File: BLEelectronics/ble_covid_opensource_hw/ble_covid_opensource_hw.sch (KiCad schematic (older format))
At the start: 35 parts, among them IC1 LTC4412xS6, IC2 LTC4054LES5-4.2#TRPBF, IC3 PCF8523T, IC4 MX25R6435FM2IL0, J1 USB_B_Micro, Q1 Si2307CDS, U1 BAT-HLD-001, U2 ESD401, U3 ESD401, U4 LP5907MFX-3.3

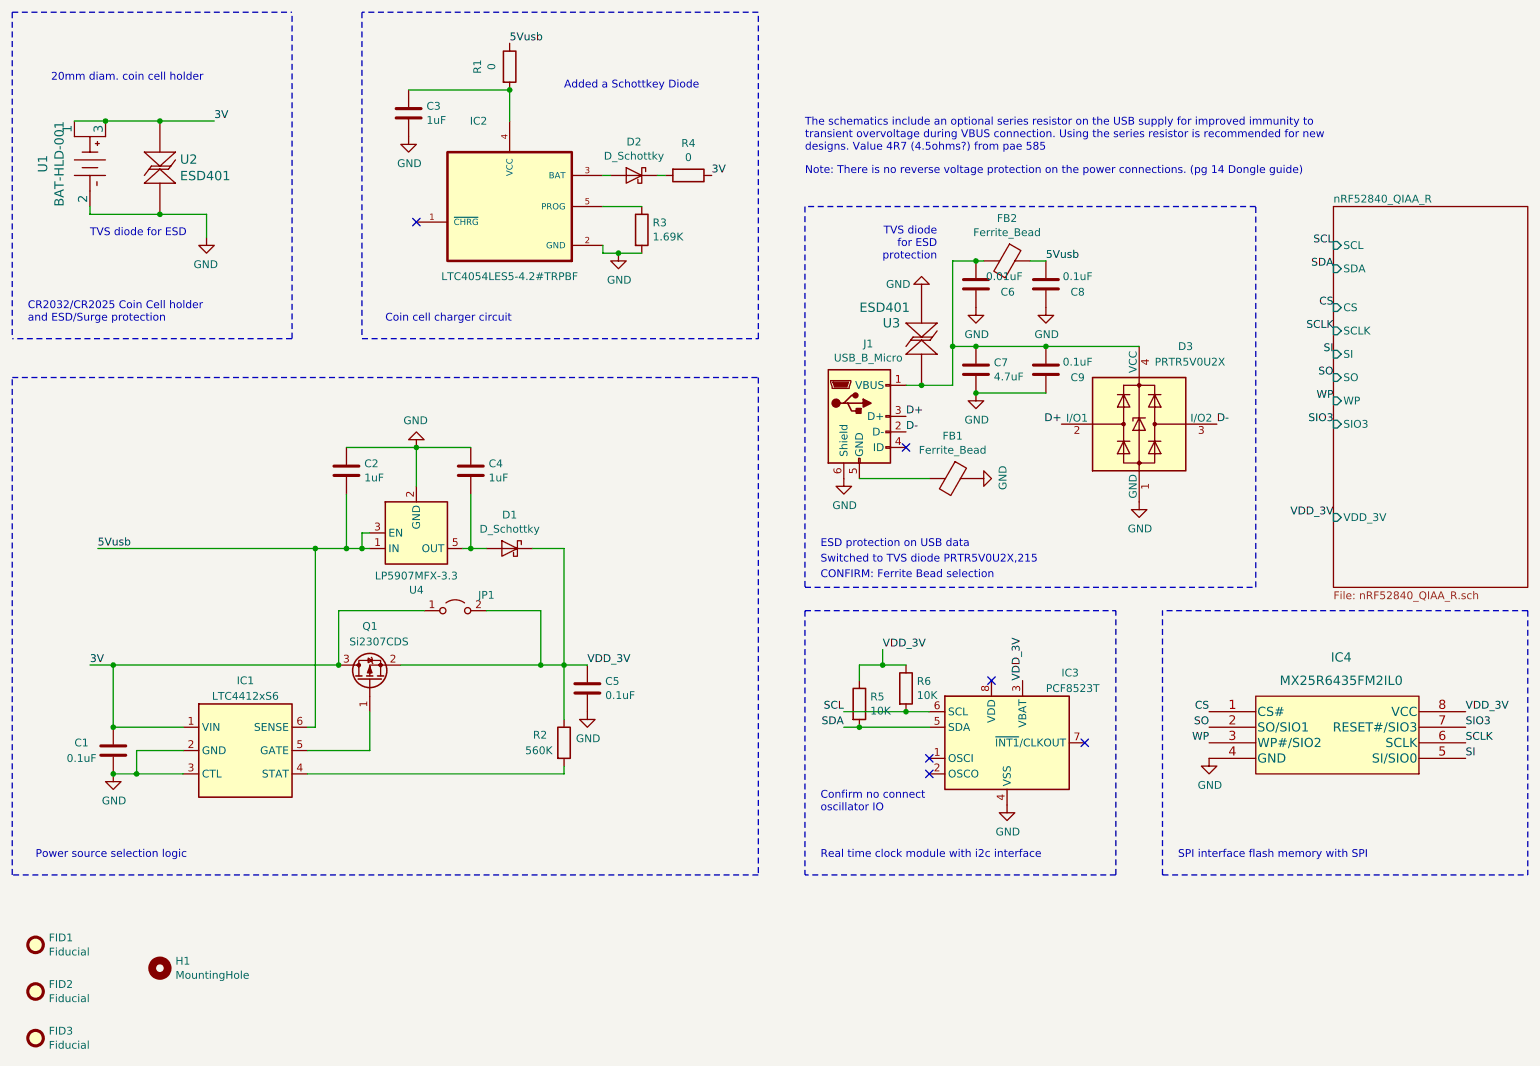
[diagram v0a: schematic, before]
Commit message: Moved power from pin 3 VBat to pin 8 Vdd on RTC. Swapped SIO3 and SDA on 1a and 1b. Changed battery footprint to allow backside routing for Flash and USB data. Todo: Unbreak MVP1B layout rerouting.
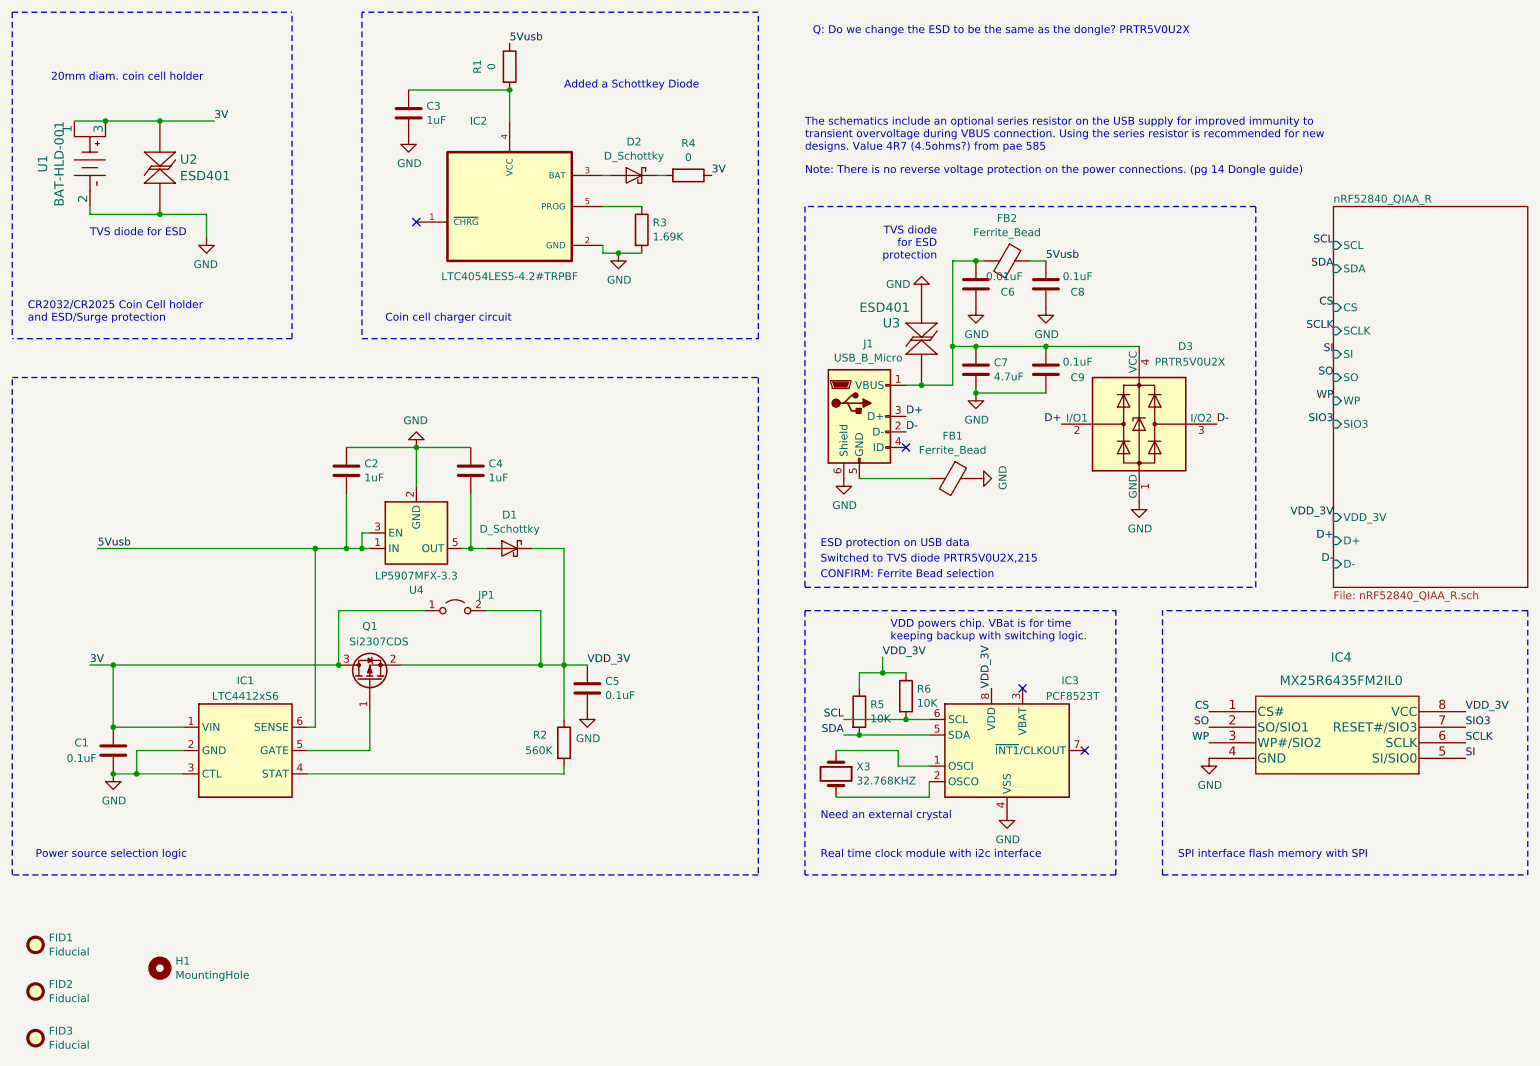
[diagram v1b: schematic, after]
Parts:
- added X3: 32.768KHZ, Crystal:Crystal_SMD_3215-2Pin_3.2x1.5mm, symbol Device:Crystal
- U1: footprint 0my_footprints:BAT-HLD-001 -> 0my_footprints:BAT-HLD-001_smallerGND
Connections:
- net VDD_3V: now also IC3.8 (VDD); no longer IC3.3 (VBAT)
- net at IC3.1 (OSCI): now also X3.1
- net at IC3.2 (OSCO): now also X3.2
- no-connect marks 6 -> 4
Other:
- note added: "Need an external crystal"
- note added: "Q: Do we change the ESD to be the same as the dongle? PRTR5V0U2X"
- note added: "VDD powers chip. VBat is for time \nkeeping backup with switching logic."
- note removed: "Confirm no connect\noscillator IO"
- moved on the sheet: IC3, R5, R6
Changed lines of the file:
@@
 F 0 "U1" H 1725 1803 60  0000 C CNN
 F 1 "BAT-HLD-001" H 1725 1697 60  0000 C CNN
-F 2 "0my_footprints:BAT-HLD-001" H 1734 1258 60  0001 C CNN
+F 2 "0my_footprints:BAT-HLD-001_smallerGND" H 1734 1258 60  0001 C CNN
 F 3 "https://linxtechnologies.com/wp/wp-content/uploads/catalog-battery-holders.pdf" H 1450 1600 60  0001 C CNN
 F 4 "Linx Technologies Inc." H -200 -100 50  0001 C CNN "MFR"
@@
 L Timer_RTC:PCF8523T IC3
 U 1 1 5E9F84DB
-P 7450 5600
-F 0 "IC3" H 7800 6050 50  0000 L CNN
-F 1 "PCF8523T" H 7700 5950 50  0000 L CNN
-F 2 "Package_SO:SOIC-8_3.9x4.9mm_P1.27mm" H 8250 5250 50  0001 C CNN
-F 3 "https://www.nxp.com/docs/en/data-sheet/PCF8523.pdf" H 7450 5600 50  0001 C CNN
-F 4 "NXP USA Inc." H 300 1500 50  0001 C CNN "MFR"
-F 5 "PCF8523T/1,118" H 300 1500 50  0001 C CNN "MPN"
-F 6 "568-5306-1-ND" H 300 1500 50  0001 C CNN "DPN"
-F 7 "-" H 300 1500 50  0001 C CNN "LCSCPN"
-F 8 "-" H 300 1500 50  0001 C CNN "SPR"
-F 9 "-" H 300 1500 50  0001 C CNN "SPN"
-F 10 "-" H 300 1500 50  0001 C CNN "SIM"
-	1    7450 5600
+P 7450 5650
+F 0 "IC3" H 7800 6100 50  0000 L CNN
+F 1 "PCF8523T" H 7700 6000 50  0000 L CNN
+F 2 "Package_SO:SOIC-8_3.9x4.9mm_P1.27mm" H 8250 5300 50  0001 C CNN
+F 3 "https://www.nxp.com/docs/en/data-sheet/PCF8523.pdf" H 7450 5650 50  0001 C CNN
+F 4 "NXP USA Inc." H 300 1550 50  0001 C CNN "MFR"
+F 5 "PCF8523T/1,118" H 300 1550 50  0001 C CNN "MPN"
+F 6 "568-5306-1-ND" H 300 1550 50  0001 C CNN "DPN"
+F 7 "-" H 300 1550 50  0001 C CNN "LCSCPN"
+F 8 "-" H 300 1550 50  0001 C CNN "SPR"
+F 9 "-" H 300 1550 50  0001 C CNN "SPN"
+F 10 "-" H 300 1550 50  0001 C CNN "SIM"
+	1    7450 5650
 	1    0    0    -1
 $EndComp
@@
 L power:GND #PWR012
 U 1 1 5EA0EA9A
-P 7450 6000
-F 0 "#PWR012" H 7450 5750 50  0001 C CNN
-F 1 "GND" H 7455 5827 50  0000 C CNN
-F 2 "" H 7450 6000 50  0001 C CNN
-F 3 "" H 7450 6000 50  0001 C CNN
-	1    7450 6000
+P 7450 6050
+F 0 "#PWR012" H 7450 5800 50  0001 C CNN
+F 1 "GND" H 7455 5877 50  0000 C CNN
+F 2 "" H 7450 6050 50  0001 C CNN
+F 3 "" H 7450 6050 50  0001 C CNN
+	1    7450 6050
 	1    0    0    -1
 $EndComp
@@
 L Device:R R6
 U 1 1 5EA074F4
-P 6800 5250
-F 0 "R6" H 6870 5296 50  0000 L CNN
-F 1 "10K" H 6870 5205 50  0000 L CNN
-F 2 "Resistor_SMD:R_0402_1005Metric" V 6730 5250 50  0001 C CNN
-F 3 "https://www.yageo.com/upload/media/product/productsearch/datasheet/rchip/PYu-RC_Group_51_RoHS_L_10.pdf" H 6800 5250 50  0001 C CNN
-F 4 "Yageo" H 350 1500 50  0001 C CNN "MFR"
-F 5 "RC0603FR-074K7L" H 350 1500 50  0001 C CNN "MPN"
-F 6 "311-4.70KHRCT-ND" H 350 1500 50  0001 C CNN "DPN"
-F 7 "-" H 350 1500 50  0001 C CNN "LCSCPN"
-F 8 "-" H 350 1500 50  0001 C CNN "SPR"
-F 9 "-" H 350 1500 50  0001 C CNN "SPN"
-F 10 "-" H 350 1500 50  0001 C CNN "SIM"
-	1    6800 5250
+P 6800 5300
+F 0 "R6" H 6870 5346 50  0000 L CNN
+F 1 "10K" H 6870 5255 50  0000 L CNN
+F 2 "Resistor_SMD:R_0402_1005Metric" V 6730 5300 50  0001 C CNN
+F 3 "https://www.yageo.com/upload/media/product/productsearch/datasheet/rchip/PYu-RC_Group_51_RoHS_L_10.pdf" H 6800 5300 50  0001 C CNN
+F 4 "Yageo" H 350 1550 50  0001 C CNN "MFR"
+F 5 "RC0603FR-074K7L" H 350 1550 50  0001 C CNN "MPN"
+F 6 "311-4.70KHRCT-ND" H 350 1550 50  0001 C CNN "DPN"
+F 7 "-" H 350 1550 50  0001 C CNN "LCSCPN"
+F 8 "-" H 350 1550 50  0001 C CNN "SPR"
+F 9 "-" H 350 1550 50  0001 C CNN "SPN"
+F 10 "-" H 350 1550 50  0001 C CNN "SIM"
+	1    6800 5300
 	1    0    0    -1
 $EndComp
@@
 L Device:R R5
 U 1 1 5EA0D031
-P 6500 5350
-F 0 "R5" H 6570 5396 50  0000 L CNN
-F 1 "10K" H 6570 5305 50  0000 L CNN
-F 2 "Resistor_SMD:R_0402_1005Metric" V 6430 5350 50  0001 C CNN
-F 3 "https://www.yageo.com/upload/media/product/productsearch/datasheet/rchip/PYu-RC_Group_51_RoHS_L_10.pdf" H 6500 5350 50  0001 C CNN
-F 4 "Yageo" H 50  1600 50  0001 C CNN "MFR"
-F 5 "RC0603FR-074K7L" H 50  1600 50  0001 C CNN "MPN"
-F 6 "311-4.70KHRCT-ND" H 50  1600 50  0001 C CNN "DPN"
-F 7 "-" H 50  1600 50  0001 C CNN "LCSCPN"
-F 8 "-" H 50  1600 50  0001 C CNN "SPR"
-F 9 "-" H 50  1600 50  0001 C CNN "SPN"
-F 10 "-" H 50  1600 50  0001 C CNN "SIM"
-	1    6500 5350
+P 6500 5400
+F 0 "R5" H 6570 5446 50  0000 L CNN
+F 1 "10K" H 6570 5355 50  0000 L CNN
+F 2 "Resistor_SMD:R_0402_1005Metric" V 6430 5400 50  0001 C CNN
+F 3 "https://www.yageo.com/upload/media/product/productsearch/datasheet/rchip/PYu-RC_Group_51_RoHS_L_10.pdf" H 6500 5400 50  0001 C CNN
+F 4 "Yageo" H 50  1650 50  0001 C CNN "MFR"
+F 5 "RC0603FR-074K7L" H 50  1650 50  0001 C CNN "MPN"
+F 6 "311-4.70KHRCT-ND" H 50  1650 50  0001 C CNN "DPN"
+F 7 "-" H 50  1650 50  0001 C CNN "LCSCPN"
+F 8 "-" H 50  1650 50  0001 C CNN "SPR"
+F 9 "-" H 50  1650 50  0001 C CNN "SPN"
+F 10 "-" H 50  1650 50  0001 C CNN "SIM"
+	1    6500 5400
 	1    0    0    -1
 $EndComp
@@
 Text Label 10400 5400 0    50   ~ 0
 VDD_3V
-Text Label 7550 5200 1    50   ~ 0
+Text Label 7350 5250 1    50   ~ 0
 VDD_3V
 Text Notes 6250 6350 0    50   ~ 0
 Real time clock module with i2c interface
-Text Label 6400 5400 2    50   ~ 0
+Text Label 6400 5450 2    50   ~ 0
 SCL
-Text Label 6400 5500 2    50   ~ 0
+Text Label 6400 5550 2    50   ~ 0
 SDA
 Text Label 8750 5500 2    50   ~ 0
@@
 Text Label 8750 5600 2    50   ~ 0
 WP
-Text Label 6650 5000 0    50   ~ 0
+Text Label 6650 5050 0    50   ~ 0
 VDD_3V
 Text Notes 1550 2350 0    50   ~ 0
 TVS diode for ESD
-Text Notes 6250 6050 0    50   ~ 0
-Confirm no connect\noscillator IO
+Text Notes 6250 6100 0    50   ~ 0
+Need an external crystal
 Text Label 10400 5600 0    50   ~ 0
 SCLK
@@
 	10800 4750 8450 4750
 Wire Wire Line
-	6950 5400 6800 5400
-Wire Wire Line
-	6800 5400 6400 5400
-Wire Wire Line
-	6500 5500 6400 5500
-Wire Wire Line
-	6500 5500 6950 5500
-Wire Wire Line
-	6500 5200 6500 5100
-Wire Wire Line
-	6500 5100 6650 5100
-Wire Wire Line
-	6650 5100 6650 5000
-Wire Wire Line
-	6650 5100 6800 5100
+	6950 5450 6800 5450
+Wire Wire Line
+	6800 5450 6400 5450
+Wire Wire Line
+	6500 5550 6400 5550
+Wire Wire Line
+	6500 5550 6950 5550
+Wire Wire Line
+	6500 5250 6500 5150
+Wire Wire Line
+	6500 5150 6650 5150
+Wire Wire Line
+	6650 5150 6650 5050
+Wire Wire Line
+	6650 5150 6800 5150
 Wire Wire Line
 	5250 1950 5200 1950
@@
 Connection ~ 4950 2450
 Connection ~ 4250 1400
-Connection ~ 6800 5400
-Connection ~ 6500 5500
-Connection ~ 6650 5100
+Connection ~ 6800 5450
+Connection ~ 6500 5550
+Connection ~ 6650 5150
 NoConn ~ 3650 2250
-NoConn ~ 6950 5800
-NoConn ~ 6950 5700
-NoConn ~ 7350 5200
 Wire Wire Line
 	1650 1600 2000 1600
@@
 F9 "SDA" I L 9550 2550 50
 F10 "VDD_3V" I L 9550 4150 50
+F11 "D+" I L 9550 4300 50
+F12 "D-" I L 9550 4450 50
 $EndSheet
 Wire Wire Line
@@
 Wire Wire Line
 	1600 4350 3000 4350
-NoConn ~ 7950 5600
+NoConn ~ 7950 5650
 Text Label 5550 1950 0    50   ~ 0
 3V
@@
 Text Label 9550 3550 2    50   ~ 0
 SIO3
+Text Notes 6200 1050 0    50   ~ 0
+Q: Do we change the ESD to be the same as the dongle? PRTR5V0U2X
+Text Notes 6700 4950 0    50   ~ 0
+VDD powers chip. VBat is for time \nkeeping backup with switching logic.
+NoConn ~ 7550 5250
+$Comp
+L Device:Crystal X?
+U 1 1 5EB2FF9A
+P 6350 5800
+AR Path="/5EA608FF/5EB2FF9A" Ref="X?"  Part="1"
+AR Path="/5EB2FF9A" Ref="X3"  Part="1"
+F 0 "X3" V 6304 5931 50  0000 L CNN
+F 1 "32.768KHZ" V 6395 5931 50  0000 L CNN
+F 2 "Crystal:Crystal_SMD_3215-2Pin_3.2x1.5mm" H 6350 5800 50  0001 C CNN
+F 3 "https://www.microcrystal.com/fileadmin/Media/Products/32kHz/Datasheet/CM7V-T1A_Low-ESR.pdf" H 6350 5800 50  0001 C CNN
+F 4 "Micro Crystal AG" V 6350 5800 50  0001 C CNN "MFR"
+F 5 "CM7VT1A-LOWESR-32.768KHZ-12.5PF-20-TA-QC" V 6350 5800 50  0001 C CNN "MPN"
+F 6 "2195-CM7VT1ALOWESR32.768KHZ12.5PF20TAQCCT-ND" V 6350 5800 50  0001 C CNN "DPN"
+	1    6350 5800
+	0    1    1    0
+$EndComp
+Wire Wire Line
+	6950 5750 6750 5750
+Wire Wire Line
+	6750 5750 6750 5650
+Wire Wire Line
+	6750 5650 6350 5650
+Wire Wire Line
+	6350 5950 6950 5950
+Wire Wire Line
+	6950 5950 6950 5850
+Text Label 9550 4450 2    50   ~ 0
+D-
+Text Label 9550 4300 2    50   ~ 0
+D+
 $EndSCHEMATC
